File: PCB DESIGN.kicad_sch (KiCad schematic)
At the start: 46 parts, among them J1 TYPE-C-31-M-12, J2 Conn_01x08_Pin, U1 AMS1117-3.3, U2 ESP32-S3-WROOM-1U-N16R8, U3 LM393AD, U4 BC547B

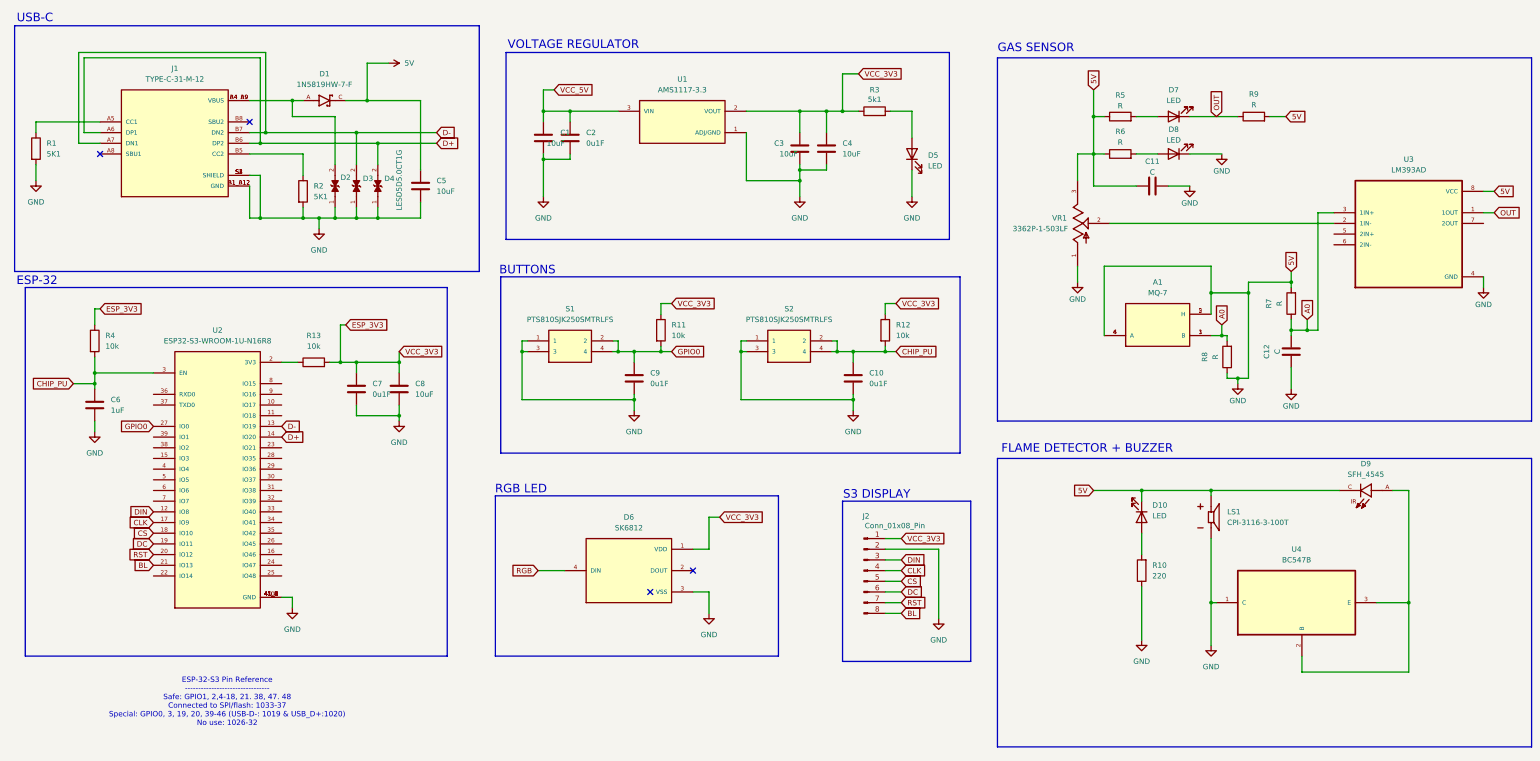
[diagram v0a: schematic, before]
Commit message: footprint placement + schematic repair
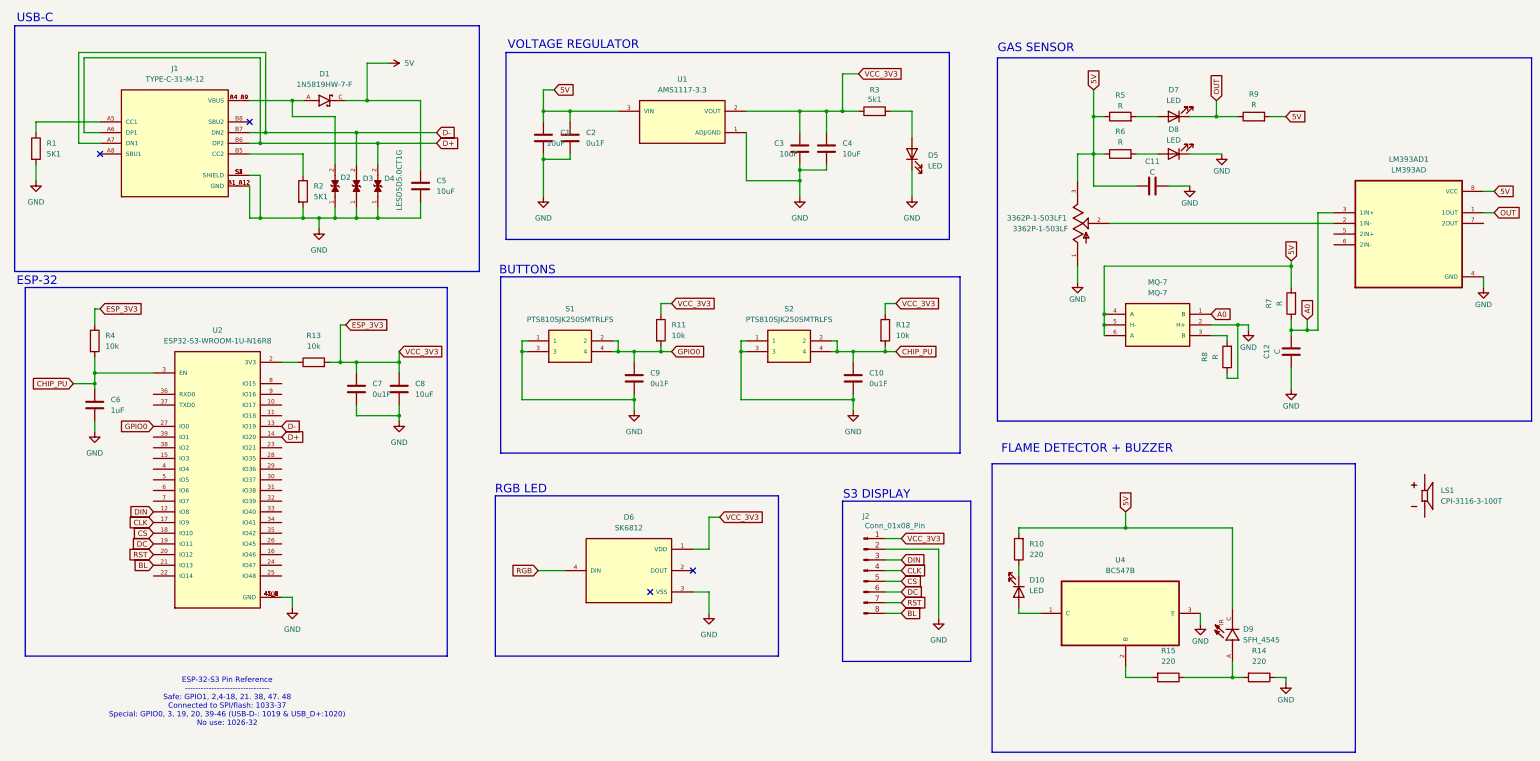
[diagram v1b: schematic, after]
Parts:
- added R14, R15: 220, Resistor_SMD:R_1206_3216Metric_Pad1.30x1.75mm_HandSolder, symbol Device:R
- 3362P-1-503LF1: renamed from VR1; footprint 3362P-1-503LF:TRIM_3362P-1-503LF -> footprints:TRIM_3362P-1-503LF
- D9: footprint SFH_4545:DIO_SFH_4545 -> footprints:DIO_SFH_4545
- LM393AD1: renamed from U3; footprint LM393AD:SOIC127P599X175-8N -> footprints:SOIC127P599X175-8N
- LS1: footprint CPI-3116-3-100T:XDCR_CPI-3116-3-100T -> footprints:XDCR_CPI-3116-3-100T
- MQ-7: renamed from A1; footprint MQ-7:XDCR_MQ-7 -> footprints:XDCR_MQ-7
- U4: footprint BC547B:TO127P254X732-3 -> footprints:TO127P254X732-3
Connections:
- net VCC_5V is gone; now on net 5V: C1.1, C2.1, U1.3 (VIN)
- net 5V: now also R10.2; no longer 3362P-1-503LF1.1, C1.2, C10.2, C11.2, C12.1, C2.2, C3.2, C4.2, C5.2, C6.2, C7.2, C8.2, C9.2, D10.1 (K), D2.1, D3.1, D4.1, D5.1 (K), D6.3 (VSS), D8.1 (K), J1.A1_B12 (GND), J1.B1_A12 (GND), J1.S1 (SHIELD), J1.S2 (SHIELD), J1.S3 (SHIELD), J1.S4 (SHIELD), J2.2 (Pin_2), LM393AD1.4 (GND), LS1.N, LS1.P, MQ-7.2 (H), R1.2, R10.1, R2.2, R8.1, S1.1, S1.3, S2.1, S2.3, U1.1 (ADJ/GND), U2.1 (GND), U2.40 (GND), U2.41_1 (GND), U2.41_2 (GND), U2.41_3 (GND), U2.41_4 (GND), U2.41_5 (GND), U2.41_6 (GND), U2.41_7 (GND), U2.41_8 (GND), U2.41_9 (GND), U4.1 (C)
- net A0: no longer MQ-7.3 (B), R8.2
- net at D10.2 (A): now also U4.1 (C); no longer R10.2
- new net: D10.1 (K), R10.1
- new net: MQ-7.3 (B), R8.2
- new net: D9.A, R14.2, R15.1
- new net: R15.2, U4.2 (B)
- new net GND: 3362P-1-503LF1.1, C1.2, C10.2, C11.2, C12.1, C2.2, C3.2, C4.2, C5.2, C6.2, C7.2, C8.2, C9.2, D2.1, D3.1, D4.1, D5.1 (K), D6.3 (VSS), D8.1 (K), J1.A1_B12 (GND), J1.B1_A12 (GND), J1.S1 (SHIELD), J1.S2 (SHIELD), J1.S3 (SHIELD), J1.S4 (SHIELD), J2.2 (Pin_2), LM393AD1.4 (GND), MQ-7.2 (H+), R1.2, R14.1, R2.2, R8.1, S1.1, S1.3, S2.1, S2.3, U1.1 (ADJ/GND), U2.1 (GND), U2.40 (GND), U2.41_1 (GND), U2.41_2 (GND), U2.41_3 (GND), U2.41_4 (GND), U2.41_5 (GND), U2.41_6 (GND), U2.41_7 (GND), U2.41_8 (GND), U2.41_9 (GND), U4.3 (E)
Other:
- moved on the sheet: D10, D9, LS1, R10, U4
